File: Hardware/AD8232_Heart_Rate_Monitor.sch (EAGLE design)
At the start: 34 parts, among them U1 AD8232

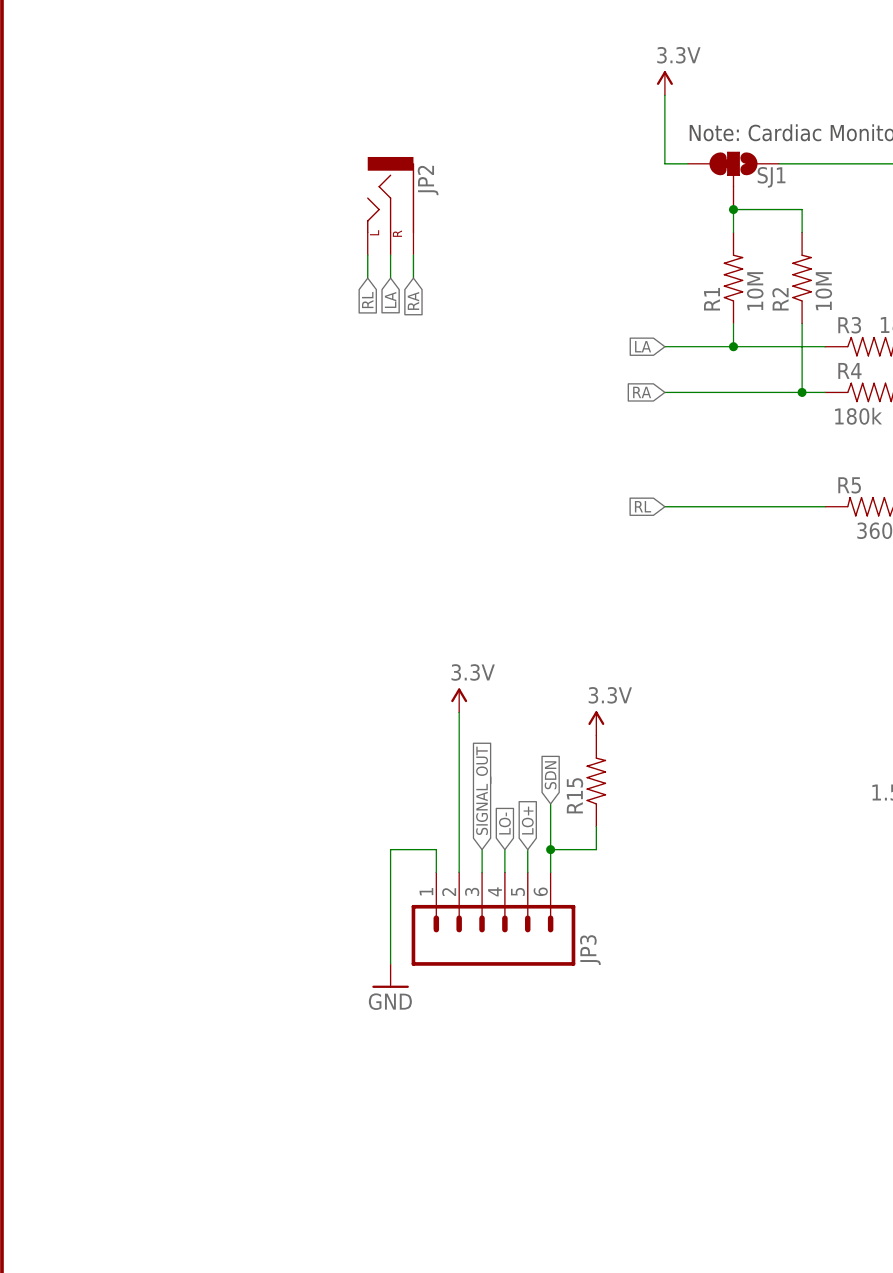
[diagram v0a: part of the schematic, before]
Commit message: added connectors for user leads, added led for some visual.
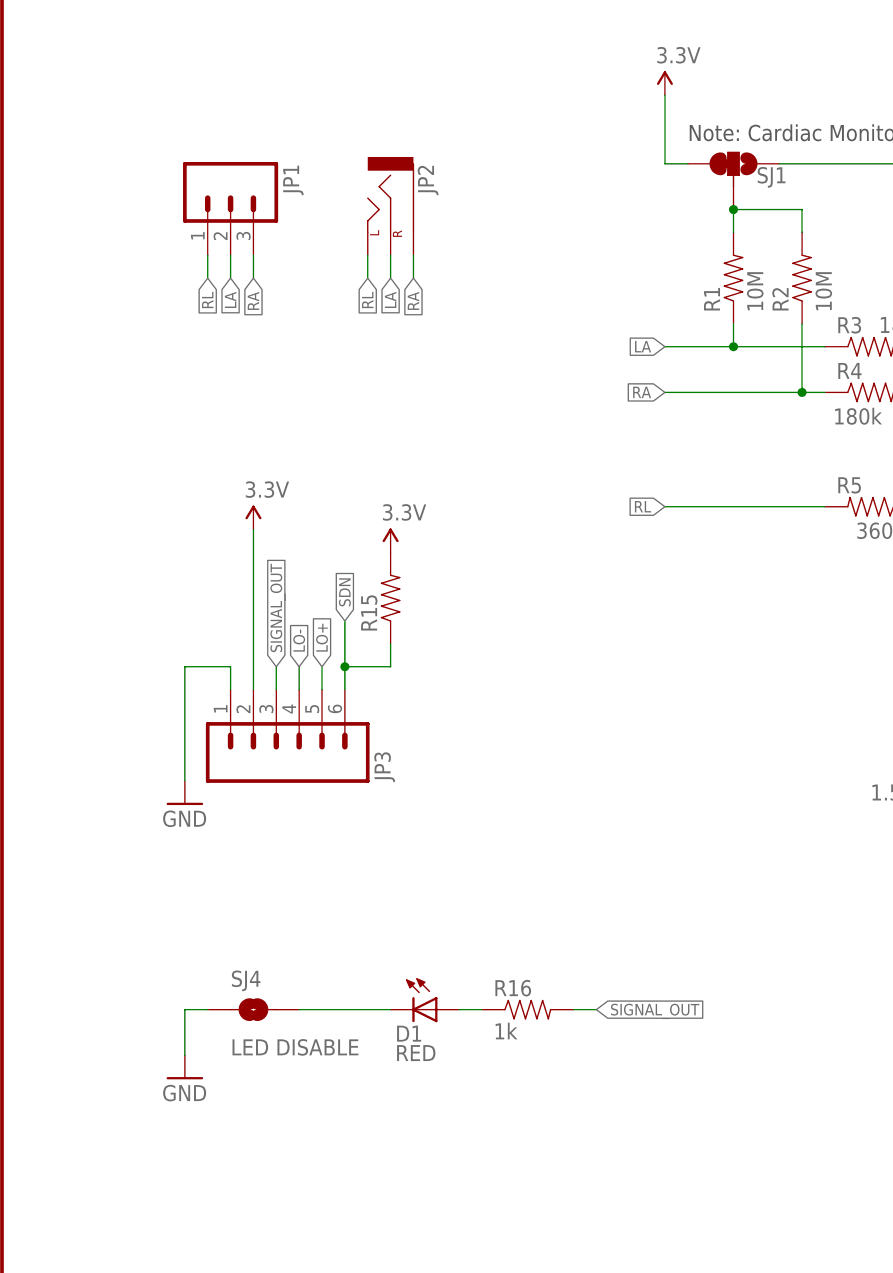
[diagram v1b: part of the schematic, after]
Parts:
- added D1: RED, SparkFun-LED:LED-RED0603
- added JP1: (no value), SparkFun-Connectors:M03PTH
- added R16: 1k, SparkFun-Resistors:1K-1%
- added SJ4: LED DISABLE, SparkFun-Passives:SOLDERJUMPERTRACE
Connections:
- new net N$10: D1.C, SJ4.2
- new net N$6: D1.A, R16.1
- net GND: now also SJ4.1
- net LA: now also JP1.2
- net RA: now also JP1.3
- net RL: now also JP1.1
- net SIGNAL_OUT: now also R16.2
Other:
- moved on the sheet: JP3, R15
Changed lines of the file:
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@@
 <part name="R15" library="SparkFun-Resistors" deviceset="10KOHM1/10W1%(0603)" device="0603"/>
 <part name="SUPPLY6" library="SparkFun-Aesthetics" deviceset="3.3V" device=""/>
+<part name="JP1" library="SparkFun-Connectors" deviceset="M03" device="PTH"/>
+<part name="R16" library="SparkFun-Resistors" deviceset="1K-1%" device="" value="1k"/>
+<part name="D1" library="SparkFun-LED" deviceset="LED-RED" device="0603" value="RED"/>
+<part name="GND4" library="SparkFun-Aesthetics" deviceset="GND" device=""/>
+<part name="SJ4" library="SparkFun-Passives" deviceset="SOLDERJUMPER" device="TRACE" value="LED DISABLE"/>
 </parts>
 <sheets>
@@
 <instance part="SUPPLY4" gate="G$1" x="203.2" y="99.06"/>
 <instance part="JP2" gate="G$1" x="43.18" y="144.78" rot="R270"/>
-<instance part="GND3" gate="1" x="43.18" y="58.42"/>
-<instance part="SUPPLY5" gate="G$1" x="50.8" y="88.9"/>
+<instance part="GND3" gate="1" x="20.32" y="78.74"/>
+<instance part="SUPPLY5" gate="G$1" x="27.94" y="109.22"/>
 <instance part="STANDOFF4" gate="G$1" x="246.38" y="25.4"/>
 <instance part="STANDOFF3" gate="G$1" x="246.38" y="30.48"/>
@@
 <instance part="LOGO2" gate="G$1" x="190.5" y="35.56"/>
 <instance part="LOGO1" gate="G$1" x="127" y="27.94"/>
-<instance part="JP3" gate="G$1" x="53.34" y="66.04" rot="MR90"/>
-<instance part="R15" gate="G$1" x="66.04" y="81.28" rot="R90"/>
-<instance part="SUPPLY6" gate="G$1" x="66.04" y="86.36"/>
+<instance part="JP3" gate="G$1" x="30.48" y="86.36" rot="MR90"/>
+<instance part="R15" gate="G$1" x="43.18" y="101.6" rot="R90"/>
+<instance part="SUPPLY6" gate="G$1" x="43.18" y="106.68"/>
+<instance part="JP1" gate="G$1" x="25.4" y="147.32" rot="R270"/>
+<instance part="R16" gate="G$1" x="58.42" y="55.88"/>
+<instance part="D1" gate="G$1" x="48.26" y="55.88" rot="R270"/>
+<instance part="GND4" gate="1" x="20.32" y="48.26"/>
+<instance part="SJ4" gate="1" x="27.94" y="55.88"/>
 </instances>
 <busses>
@@
 <segment>
 <pinref part="GND3" gate="1" pin="GND"/>
-<wire x1="43.18" y1="60.96" x2="43.18" y2="73.66" width="0.1524" layer="91"/>
-<wire x1="43.18" y1="73.66" x2="48.26" y2="73.66" width="0.1524" layer="91"/>
+<wire x1="20.32" y1="81.28" x2="20.32" y2="93.98" width="0.1524" layer="91"/>
+<wire x1="20.32" y1="93.98" x2="25.4" y2="93.98" width="0.1524" layer="91"/>
 <pinref part="JP3" gate="G$1" pin="1"/>
-<wire x1="48.26" y1="71.12" x2="48.26" y2="73.66" width="0.1524" layer="91"/>
+<wire x1="25.4" y1="91.44" x2="25.4" y2="93.98" width="0.1524" layer="91"/>
+</segment>
+<segment>
+<pinref part="SJ4" gate="1" pin="1"/>
+<pinref part="GND4" gate="1" pin="GND"/>
+<wire x1="20.32" y1="50.8" x2="20.32" y2="55.88" width="0.1524" layer="91"/>
+<wire x1="20.32" y1="55.88" x2="22.86" y2="55.88" width="0.1524" layer="91"/>
 </segment>
 </net>
@@
 <segment>
 <pinref part="JP3" gate="G$1" pin="3"/>
-<wire x1="53.34" y1="71.12" x2="53.34" y2="73.66" width="0.1524" layer="91"/>
-<label x="53.34" y="73.66" size="1.27" layer="95" rot="R90" xref="yes"/>
+<wire x1="30.48" y1="91.44" x2="30.48" y2="93.98" width="0.1524" layer="91"/>
+<label x="30.48" y="93.98" size="1.27" layer="95" rot="R90" xref="yes"/>
+</segment>
+<segment>
+<wire x1="66.04" y1="55.88" x2="63.5" y2="55.88" width="0.1524" layer="91"/>
+<label x="66.04" y="55.88" size="1.27" layer="95" xref="yes"/>
+<pinref part="R16" gate="G$1" pin="2"/>
 </segment>
 </net>
@@
 <label x="43.18" y="137.16" size="1.27" layer="95" rot="R270" xref="yes"/>
 </segment>
+<segment>
+<wire x1="25.4" y1="139.7" x2="25.4" y2="137.16" width="0.1524" layer="91"/>
+<label x="25.4" y="137.16" size="1.27" layer="95" rot="R270" xref="yes"/>
+<pinref part="JP1" gate="G$1" pin="2"/>
+</segment>
 </net>
 <net name="RA" class="0">
@@
 <wire x1="45.72" y1="139.7" x2="45.72" y2="137.16" width="0.1524" layer="91"/>
 <label x="45.72" y="137.16" size="1.27" layer="95" rot="R270" xref="yes"/>
+</segment>
+<segment>
+<wire x1="27.94" y1="139.7" x2="27.94" y2="137.16" width="0.1524" layer="91"/>
+<label x="27.94" y="137.16" size="1.27" layer="95" rot="R270" xref="yes"/>
+<pinref part="JP1" gate="G$1" pin="3"/>
 </segment>
 </net>
@@
 <pinref part="JP3" gate="G$1" pin="2"/>
 <pinref part="SUPPLY5" gate="G$1" pin="3.3V"/>
-<wire x1="50.8" y1="88.9" x2="50.8" y2="71.12" width="0.1524" layer="91"/>
+<wire x1="27.94" y1="109.22" x2="27.94" y2="91.44" width="0.1524" layer="91"/>
 </segment>
 <segment>
@@
 </segment>
 <segment>
-<wire x1="58.42" y1="71.12" x2="58.42" y2="73.66" width="0.1524" layer="91"/>
-<label x="58.42" y="73.66" size="1.27" layer="95" rot="R90" xref="yes"/>
+<wire x1="35.56" y1="91.44" x2="35.56" y2="93.98" width="0.1524" layer="91"/>
+<label x="35.56" y="93.98" size="1.27" layer="95" rot="R90" xref="yes"/>
 <pinref part="JP3" gate="G$1" pin="5"/>
 </segment>
@@
 </segment>
 <segment>
-<wire x1="55.88" y1="71.12" x2="55.88" y2="73.66" width="0.1524" layer="91"/>
-<label x="55.88" y="73.66" size="1.27" layer="95" rot="R90" xref="yes"/>
+<wire x1="33.02" y1="91.44" x2="33.02" y2="93.98" width="0.1524" layer="91"/>
+<label x="33.02" y="93.98" size="1.27" layer="95" rot="R90" xref="yes"/>
 <pinref part="JP3" gate="G$1" pin="4"/>
 </segment>
@@
 <label x="40.64" y="137.16" size="1.27" layer="95" rot="R270" xref="yes"/>
 </segment>
+<segment>
+<wire x1="22.86" y1="139.7" x2="22.86" y2="137.16" width="0.1524" layer="91"/>
+<label x="22.86" y="137.16" size="1.27" layer="95" rot="R270" xref="yes"/>
+<pinref part="JP1" gate="G$1" pin="1"/>
+</segment>
 </net>
 <net name="SDN" class="0">
 <segment>
-<wire x1="60.96" y1="71.12" x2="60.96" y2="73.66" width="0.1524" layer="91"/>
-<label x="60.96" y="78.74" size="1.27" layer="95" rot="R90" xref="yes"/>
+<wire x1="38.1" y1="91.44" x2="38.1" y2="93.98" width="0.1524" layer="91"/>
+<label x="38.1" y="99.06" size="1.27" layer="95" rot="R90" xref="yes"/>
 <pinref part="JP3" gate="G$1" pin="6"/>
-<wire x1="60.96" y1="73.66" x2="60.96" y2="78.74" width="0.1524" layer="91"/>
-<wire x1="60.96" y1="73.66" x2="66.04" y2="73.66" width="0.1524" layer="91"/>
-<wire x1="66.04" y1="73.66" x2="66.04" y2="76.2" width="0.1524" layer="91"/>
+<wire x1="38.1" y1="93.98" x2="38.1" y2="99.06" width="0.1524" layer="91"/>
+<wire x1="38.1" y1="93.98" x2="43.18" y2="93.98" width="0.1524" layer="91"/>
+<wire x1="43.18" y1="93.98" x2="43.18" y2="96.52" width="0.1524" layer="91"/>
 <pinref part="R15" gate="G$1" pin="1"/>
-<junction x="60.96" y="73.66"/>
+<junction x="38.1" y="93.98"/>
 </segment>
 <segment>
@@
 </segment>
 </net>
+<net name="N$6" class="0">
+<segment>
+<pinref part="R16" gate="G$1" pin="1"/>
+<pinref part="D1" gate="G$1" pin="A"/>
+<wire x1="50.8" y1="55.88" x2="53.34" y2="55.88" width="0.1524" layer="91"/>
+</segment>
+</net>
+<net name="N$10" class="0">
+<segment>
+<pinref part="D1" gate="G$1" pin="C"/>
+<pinref part="SJ4" gate="1" pin="2"/>
+<wire x1="43.18" y1="55.88" x2="33.02" y2="55.88" width="0.1524" layer="91"/>
+</segment>
+</net>
